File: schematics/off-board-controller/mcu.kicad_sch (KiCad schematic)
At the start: 4 parts, among them J1 programmer, U4 STM32L476RGTx

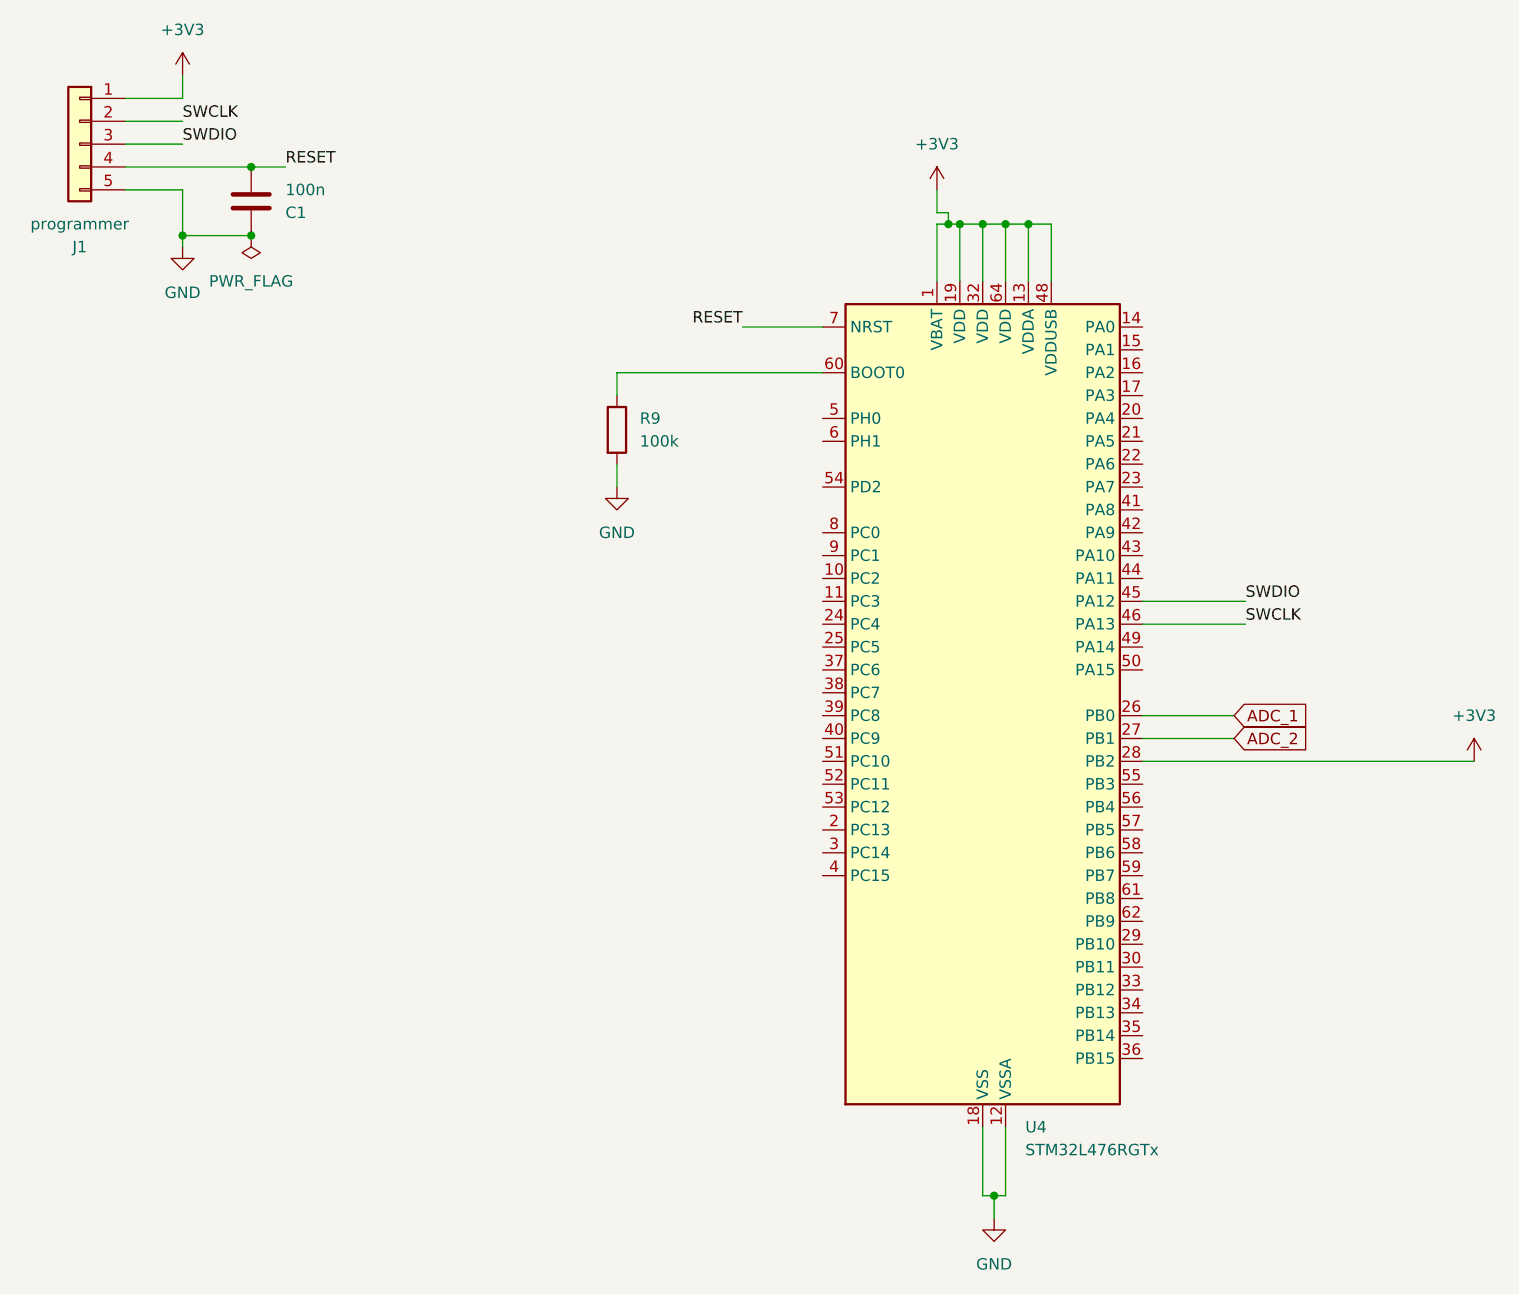
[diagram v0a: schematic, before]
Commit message: off-board: created schematic
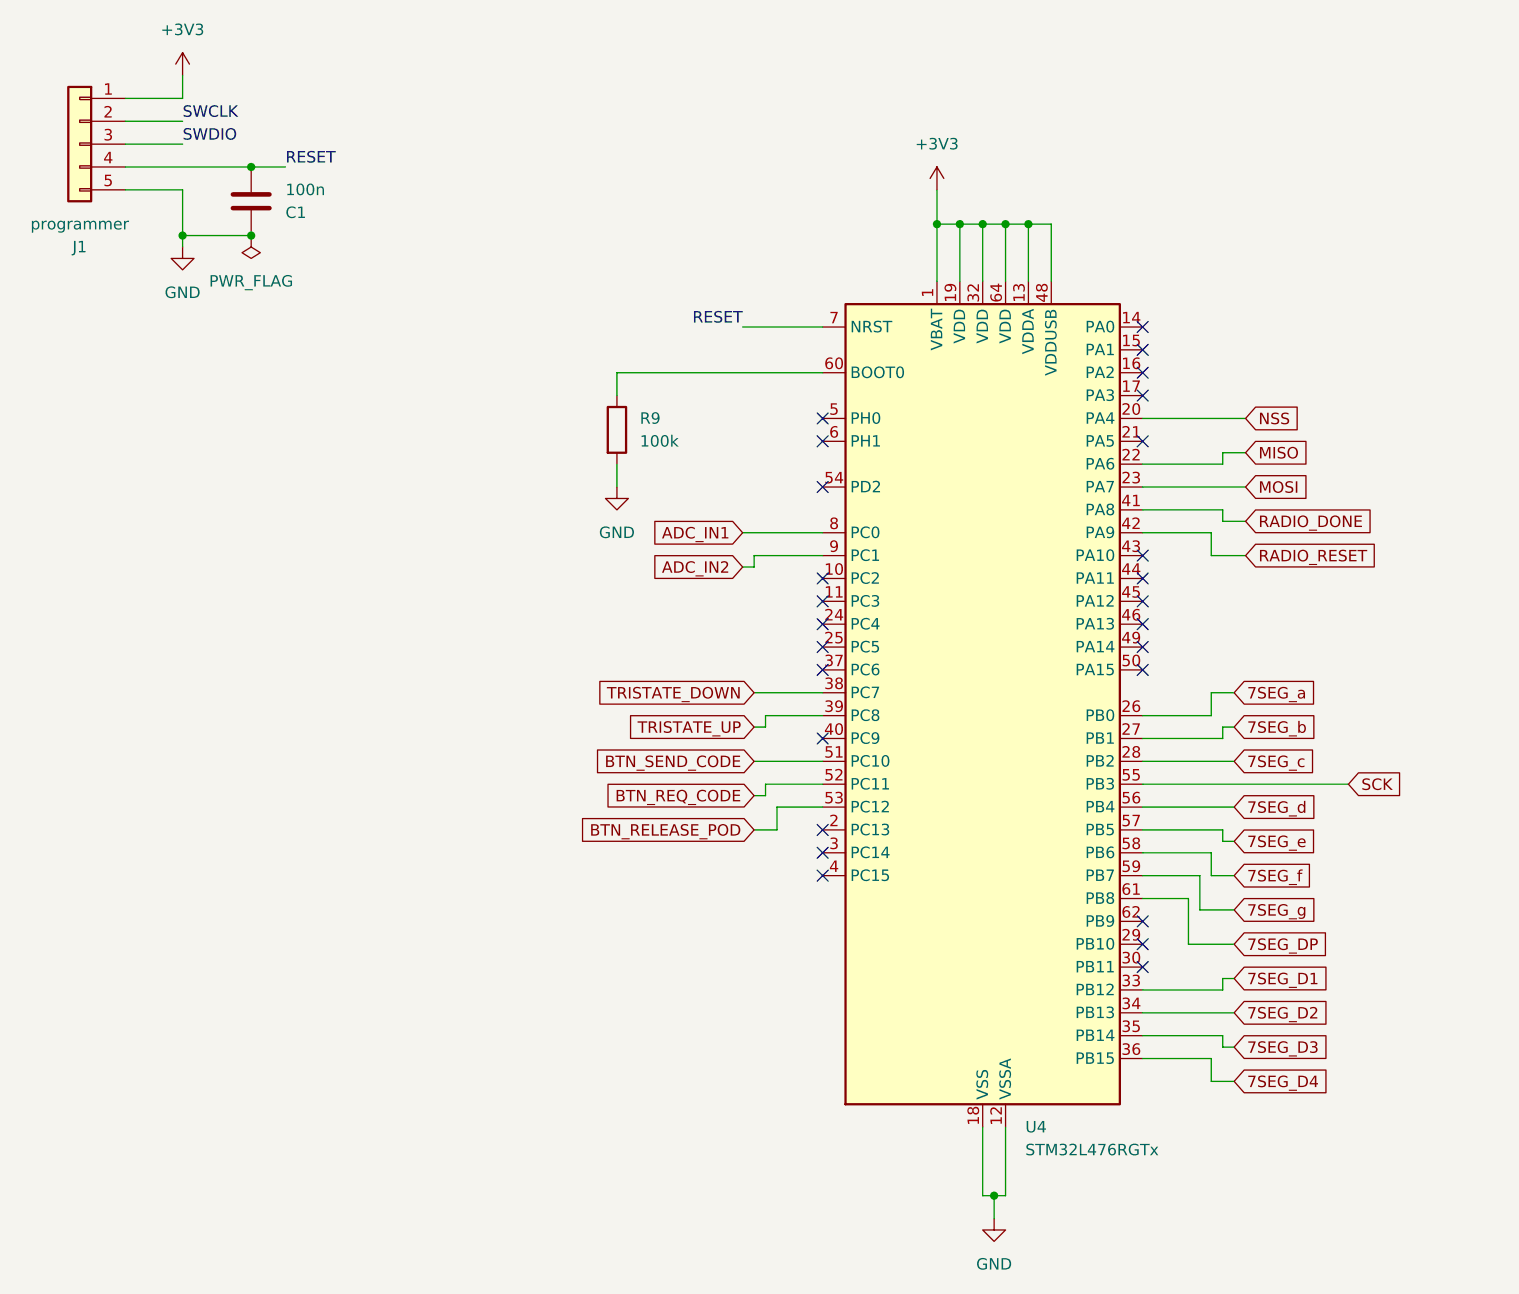
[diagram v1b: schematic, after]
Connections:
- net +3V3: no longer U4.28 (PB2)
- net SWCLK: no longer U4.46 (PA13)
- net SWDIO: no longer U4.45 (PA12)
- net NSS: now reaches U4.20 (PA4)
- net MISO: now reaches U4.22 (PA6)
- net MOSI: now reaches U4.23 (PA7)
- net 7SEG_D1: now reaches U4.33 (PB12)
- net 7SEG_D2: now reaches U4.34 (PB13)
- net 7SEG_D3: now reaches U4.35 (PB14)
- net 7SEG_D4: now reaches U4.36 (PB15)
- net TRISTATE_DOWN: now reaches U4.38 (PC7)
- net TRISTATE_UP: now reaches U4.39 (PC8)
- net RADIO_DONE: now reaches U4.41 (PA8)
- net RADIO_RESET: now reaches U4.42 (PA9)
- net BTN_SEND_CODE: now reaches U4.51 (PC10)
- net BTN_REQ_CODE: now reaches U4.52 (PC11)
- net BTN_RELEASE_POD: now reaches U4.53 (PC12)
- net SCK: now reaches U4.55 (PB3)
- net 7SEG_d: now reaches U4.56 (PB4)
- net 7SEG_e: now reaches U4.57 (PB5)
- net 7SEG_f: now reaches U4.58 (PB6)
- net 7SEG_g: now reaches U4.59 (PB7)
- net 7SEG_DP: now reaches U4.61 (PB8)
- net ADC_IN1: now reaches U4.8 (PC0)
- net ADC_IN2: now reaches U4.9 (PC1)
- net ADC_1 renamed 7SEG_a
- net ADC_2 renamed 7SEG_b
- new net 7SEG_c: U4.28 (PB2)
- no-connect marks 0 -> 26
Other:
- title: (none) -> Off-board Controller

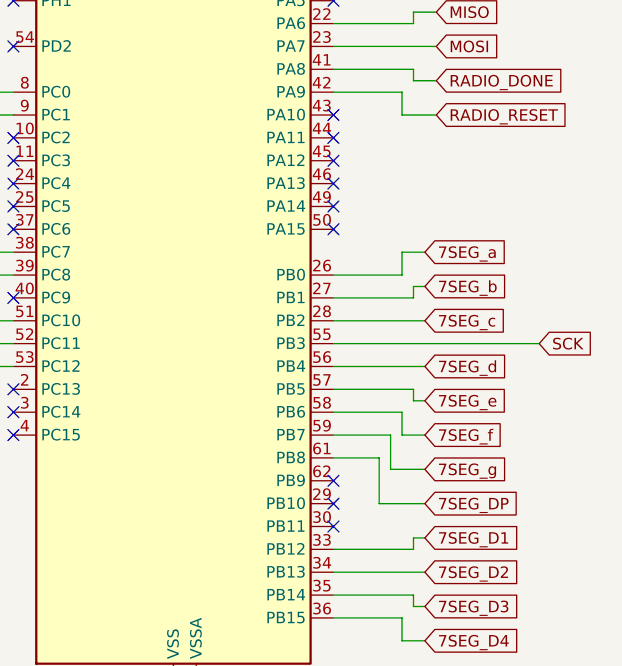
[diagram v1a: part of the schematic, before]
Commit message: off-board: added SWCLK and SWDIO needed for the programmer, resolved conflicts
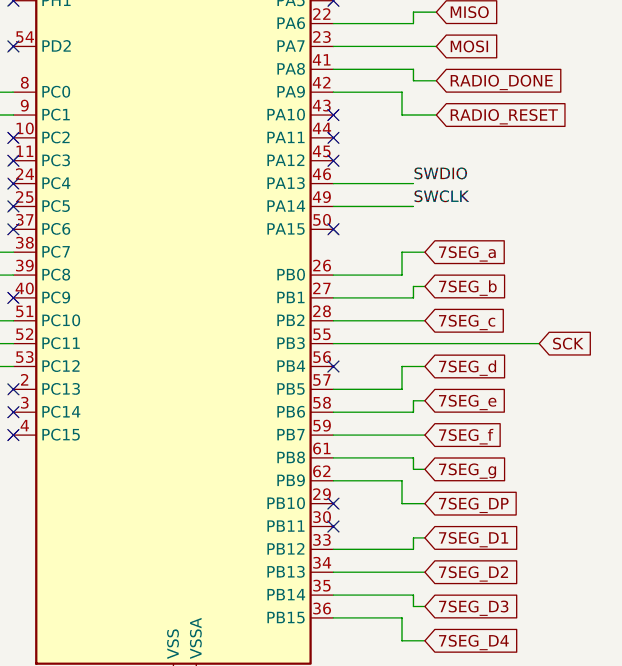
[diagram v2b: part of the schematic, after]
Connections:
- net 7SEG_DP: now also U4.62 (PB9); no longer U4.61 (PB8)
- net 7SEG_d: now also U4.57 (PB5); no longer U4.56 (PB4)
- net 7SEG_e: now also U4.58 (PB6); no longer U4.57 (PB5)
- net 7SEG_f: now also U4.59 (PB7); no longer U4.58 (PB6)
- net 7SEG_g: now also U4.61 (PB8); no longer U4.59 (PB7)
- net SWCLK: now also U4.49 (PA14)
- net SWDIO: now also U4.46 (PA13)
- no-connect marks 26 -> 24
